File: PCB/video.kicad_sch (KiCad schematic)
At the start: 2 parts, among them U14 KM416x254, U15 KM416x254

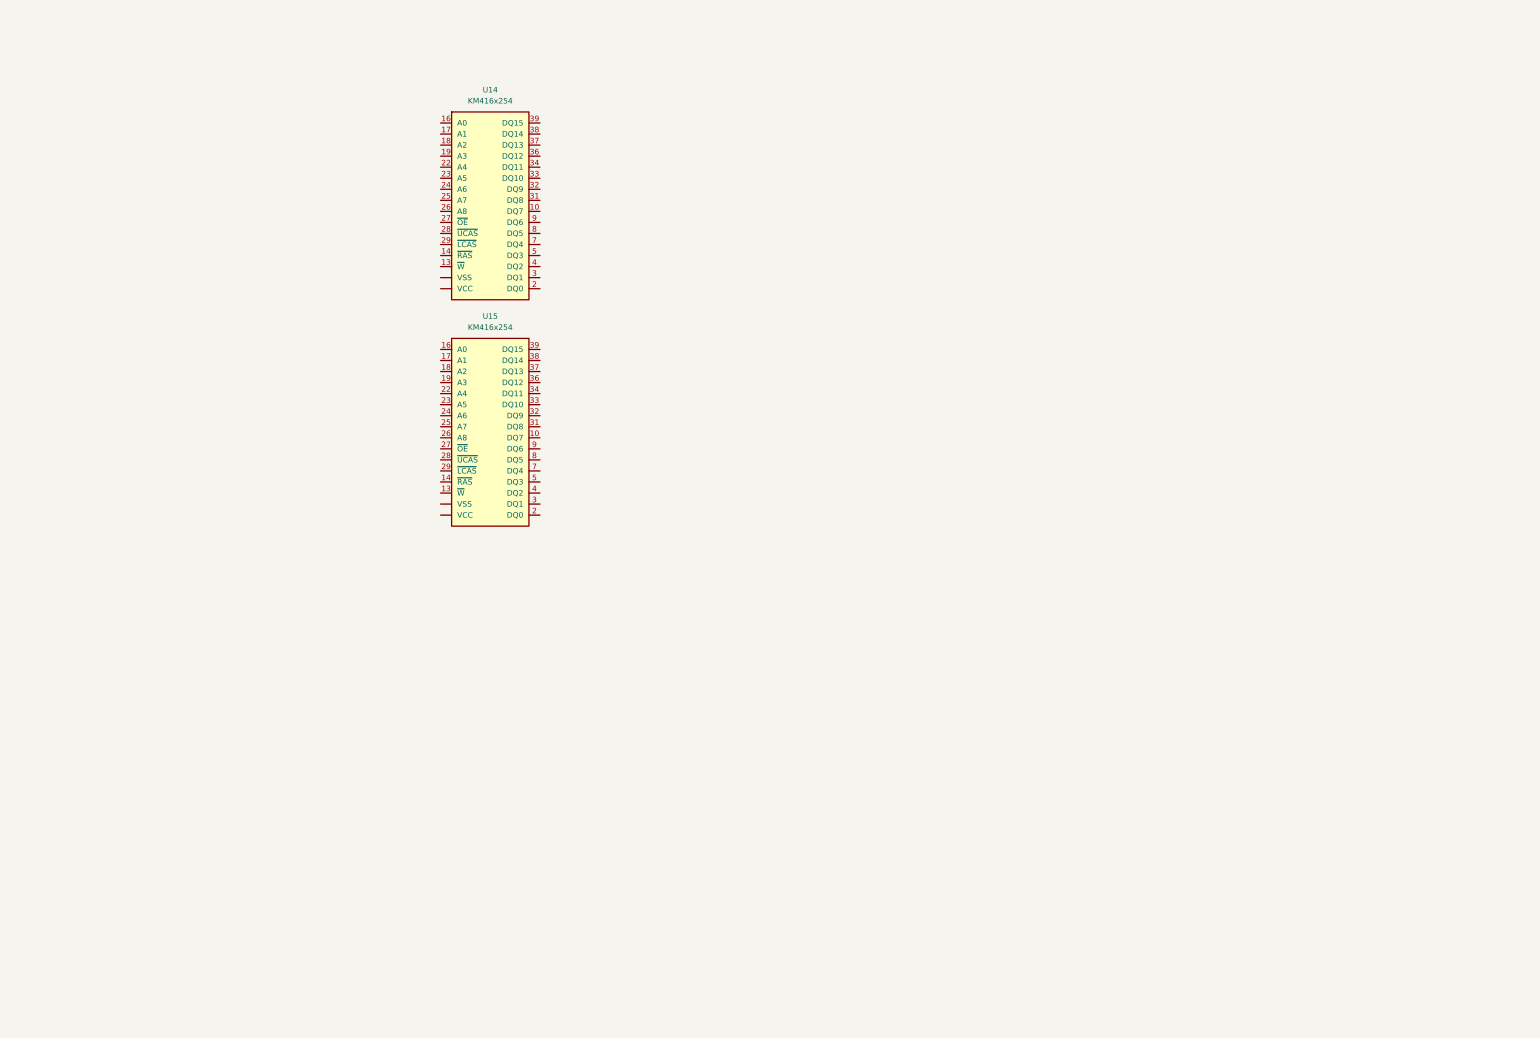
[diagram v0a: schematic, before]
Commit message: adding video chip and support bits
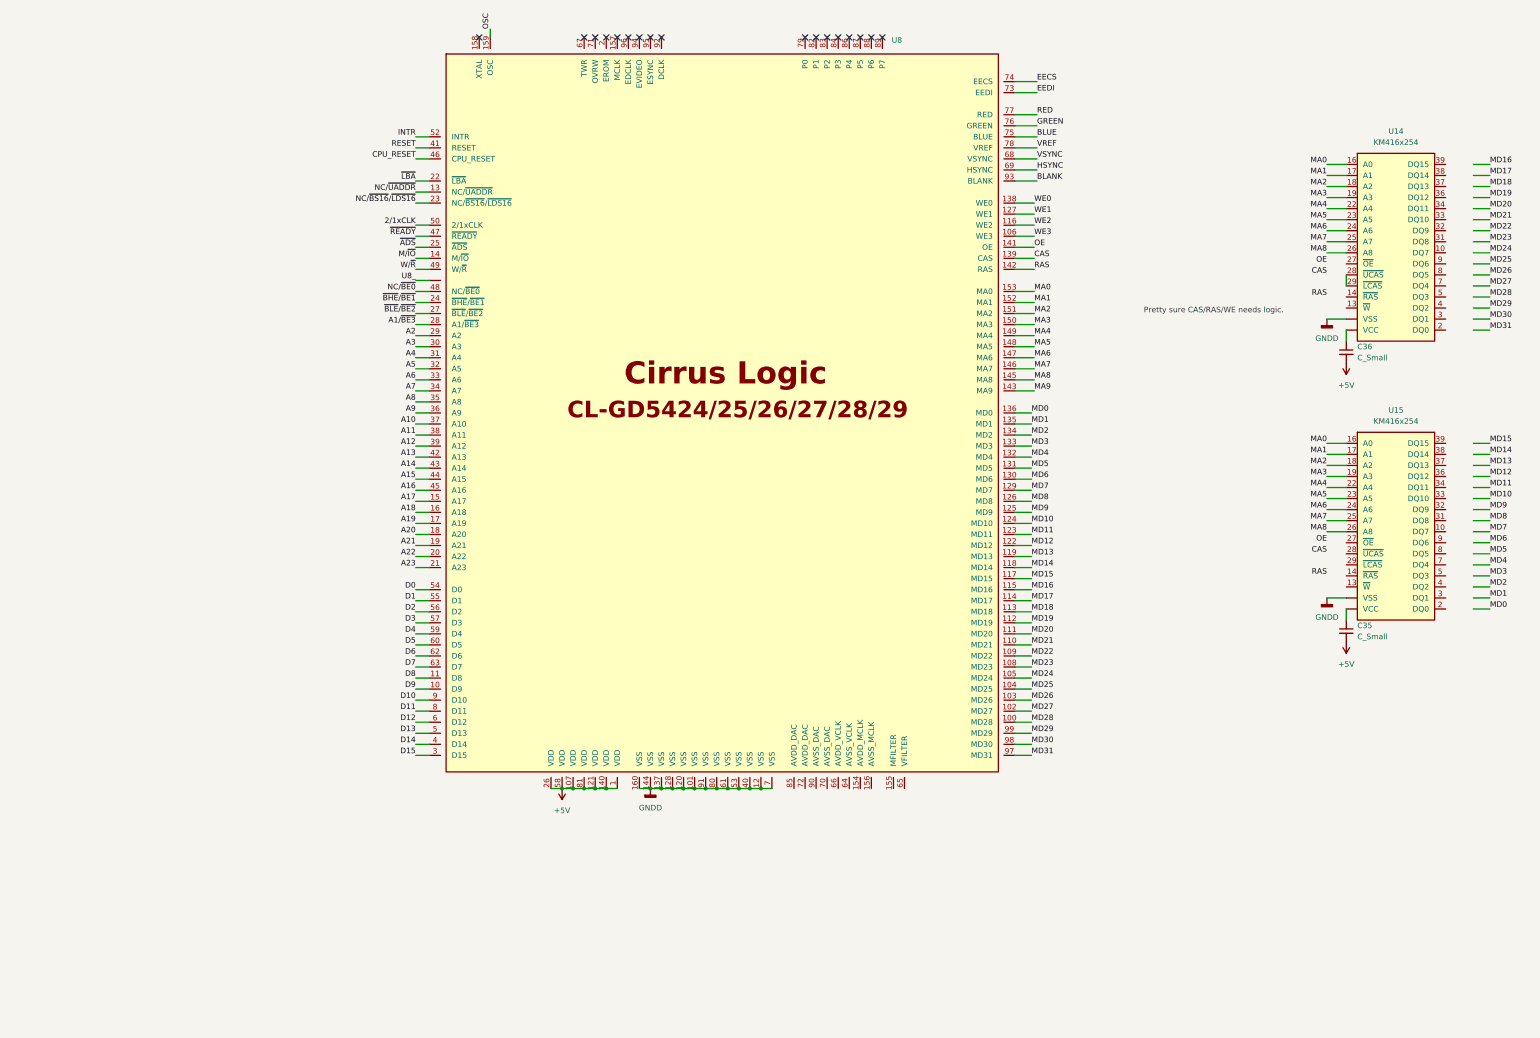
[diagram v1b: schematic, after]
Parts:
- added C35, C36: C_Small, symbol Device:C_Small
- added U8: CL-GD5428-LOCALBUS, Package_QFP:PQFP-160_28x28mm_P0.65mm, symbol CL-GD54xx:CL-GD542x
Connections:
- net at U15.1,6,20 (VCC): now also C35.1
- net MA0: now reaches U15.16 (A0)
- net MA0: now also U14.16 (A0), U8.153 (MA0)
- net MA1: now reaches U15.17 (A1)
- net MA1: now also U14.17 (A1), U8.152 (MA1)
- net MA2: now reaches U15.18 (A2)
- net MA2: now also U14.18 (A2), U8.151 (MA2)
- net MA3: now reaches U15.19 (A3)
- net MA3: now also U14.19 (A3), U8.150 (MA3)
- net GNDD: now reaches U15.21,35,40 (VSS)
- net GNDD: now also U14.21,35,40 (VSS), U8.101 (VSS), U8.12 (VSS), U8.120 (VSS), U8.128 (VSS), U8.137 (VSS), U8.144 (VSS), U8.160 (VSS), U8.40 (VSS), U8.53 (VSS), U8.61 (VSS), U8.7 (VSS), U8.80 (VSS), U8.91 (VSS)
- net MA4: now reaches U15.22 (A4)
- net MA4: now also U14.22 (A4), U8.149 (MA4)
- net MA5: now reaches U15.23 (A5)
- net MA5: now also U14.23 (A5), U8.148 (MA5)
- net MA6: now reaches U15.24 (A6)
- net MA6: now also U14.24 (A6), U8.147 (MA6)
- net MA7: now reaches U15.25 (A7)
- net MA7: now also U14.25 (A7), U8.146 (MA7)
- net MA8: now reaches U15.26 (A8)
- net MA8: now also U14.26 (A8), U8.145 (MA8)
- net at U14.1,6,20 (VCC): now also C36.1
- net at U14.28 (~{UCAS}): now also U14.29 (~{LCAS})
- new net +5V: C35.2, C36.2, U8.1 (VDD), U8.107 (VDD), U8.121 (VDD), U8.140 (VDD), U8.26 (VDD), U8.58 (VDD), U8.81 (VDD)
- new net 2/1xCLK: U8.50 (2/1xCLK)
- new net A1/~{BE3}: U8.28 (A1/~{BE3})
- new net A10: U8.37 (A10)
- new net A11: U8.38 (A11)
- new net A12: U8.39 (A12)
- new net A13: U8.42 (A13)
- new net A14: U8.43 (A14)
- new net A15: U8.44 (A15)
- new net A16: U8.45 (A16)
- new net A17: U8.15 (A17)
- new net A18: U8.16 (A18)
- new net A19: U8.17 (A19)
- new net A2: U8.29 (A2)
- new net A20: U8.18 (A20)
- new net A21: U8.19 (A21)
- new net A22: U8.20 (A22)
- new net A23: U8.21 (A23)
- new net A3: U8.30 (A3)
- new net A4: U8.31 (A4)
- new net A5: U8.32 (A5)
- new net A6: U8.33 (A6)
- new net A7: U8.34 (A7)
- new net A8: U8.35 (A8)
- new net A9: U8.36 (A9)
- new net BLANK: U8.93 (BLANK)
- new net BLUE: U8.75 (BLUE)
- new net CAS: U8.139 (CAS)
- new net CPU_RESET: U8.46 (CPU_RESET)
- new net D0: U8.54 (D0)
- new net D1: U8.55 (D1)
- new net D10: U8.9 (D10)
- new net D11: U8.8 (D11)
- new net D12: U8.6 (D12)
- new net D13: U8.5 (D13)
- new net D14: U8.4 (D14)
- new net D15: U8.3 (D15)
- new net D2: U8.56 (D2)
- new net D3: U8.57 (D3)
- new net D4: U8.59 (D4)
- new net D5: U8.60 (D5)
- new net D6: U8.62 (D6)
- new net D7: U8.63 (D7)
- new net D8: U8.11 (D8)
- new net D9: U8.10 (D9)
- new net EECS: U8.74 (EECS)
- new net EEDI: U8.73 (EEDI)
- new net GREEN: U8.76 (GREEN)
- new net HSYNC: U8.69 (HSYNC)
- new net INTR: U8.52 (INTR)
- new net M/~{IO}: U8.14 (M/~{IO})
- new net MA9: U8.143 (MA9)
- new net MD0: U8.136 (MD0)
- new net MD1: U8.135 (MD1)
- new net MD10: U8.124 (MD10)
- new net MD11: U8.123 (MD11)
- new net MD12: U8.122 (MD12)
- new net MD13: U8.119 (MD13)
- new net MD14: U8.118 (MD14)
- new net MD15: U8.117 (MD15)
- new net MD16: U8.115 (MD16)
- new net MD17: U8.114 (MD17)
- new net MD18: U8.113 (MD18)
- new net MD19: U8.112 (MD19)
- new net MD2: U8.134 (MD2)
- new net MD20: U8.111 (MD20)
- new net MD21: U8.110 (MD21)
- new net MD22: U8.109 (MD22)
- new net MD23: U8.108 (MD23)
- new net MD24: U8.105 (MD24)
- new net MD25: U8.104 (MD25)
- new net MD26: U8.103 (MD26)
- new net MD27: U8.102 (MD27)
- new net MD28: U8.100 (MD28)
- new net MD29: U8.99 (MD29)
- new net MD3: U8.133 (MD3)
- new net MD30: U8.98 (MD30)
- new net MD31: U8.97 (MD31)
- new net MD4: U8.132 (MD4)
- new net MD5: U8.131 (MD5)
- new net MD6: U8.130 (MD6)
- new net MD7: U8.129 (MD7)
- new net MD8: U8.126 (MD8)
- new net MD9: U8.125 (MD9)
- new net NC/~{BE0}: U8.48 (NC/~{BE0})
- new net NC/~{BS16}/~{LDS16}: U8.23 (NC/~{BS16}/~{LDS16})
- new net NC/~{UADDR}: U8.13 (NC/~{UADDR})
- new net OE: U8.141 (OE)
- new net OSC: U8.159 (OSC)
- new net RAS: U8.142 (RAS)
- new net RED: U8.77 (RED)
- new net RESET: U8.41 (RESET)
- new net U8_: U8.
- new net VREF: U8.78 (VREF)
- new net VSYNC: U8.68 (VSYNC)
- new net W/~{R}: U8.49 (W/~{R})
- new net WE0: U8.138 (WE0)
- new net WE1: U8.127 (WE1)
- new net WE2: U8.116 (WE2)
- new net WE3: U8.106 (WE3)
- new net ~{ADS}: U8.25 (~{ADS})
- new net ~{BHE}/~{BE1}: U8.24 (~{BHE}/~{BE1})
- new net ~{BLE}/~{BE2}: U8.27 (~{BLE}/~{BE2})
- new net ~{LBA}: U8.22 (~{LBA})
- new net ~{READY}: U8.47 (~{READY})
- no-connect marks 0 -> 17
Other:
- note added: "Pretty sure CAS/RAS/WE needs logic."
- moved on the sheet: U14, U15

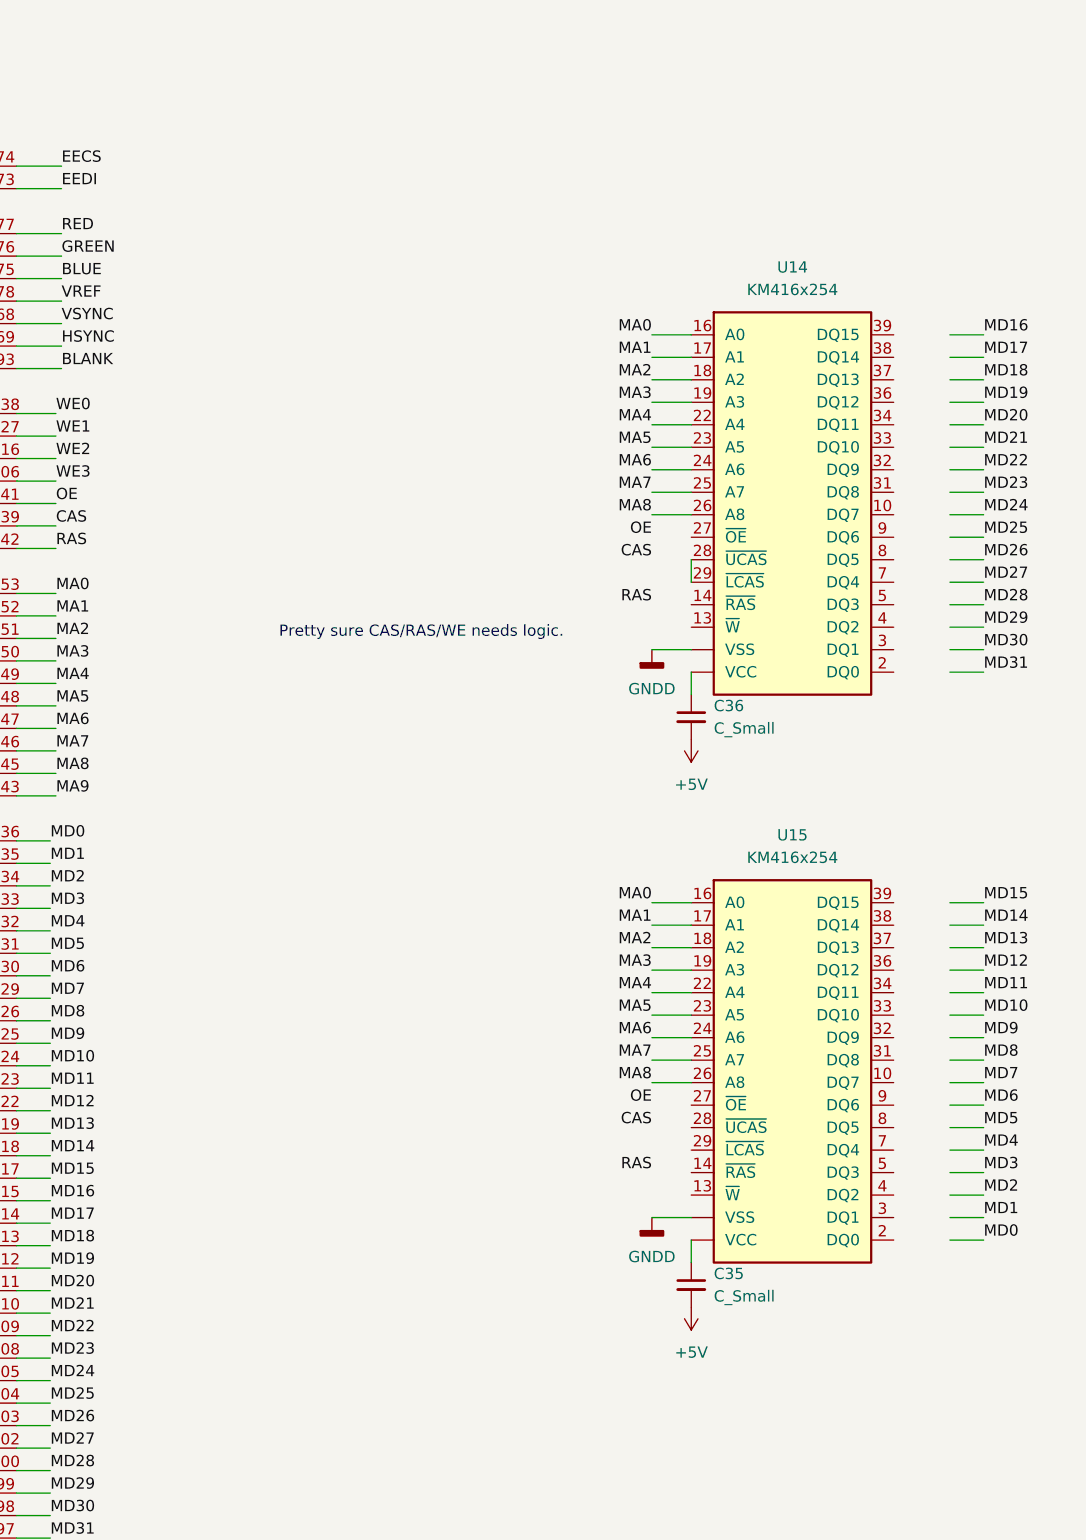
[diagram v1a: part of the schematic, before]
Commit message: dove into CAS/RAS/OE/WE muxing for Multi-cas 256x16 mem devices
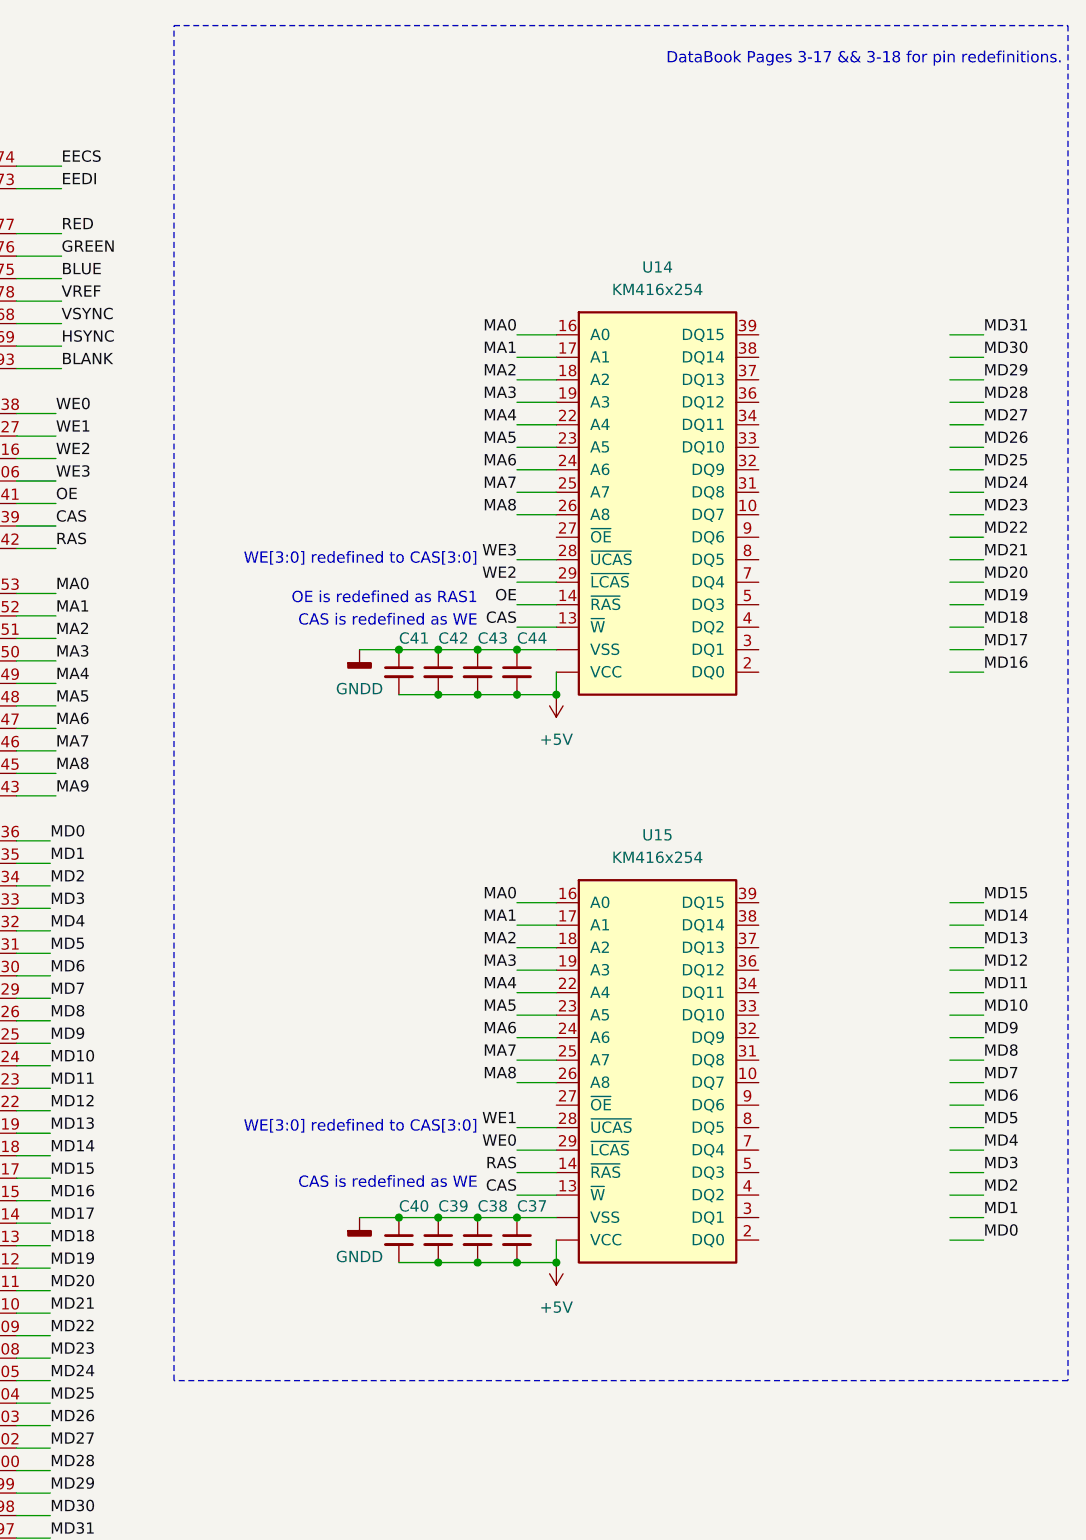
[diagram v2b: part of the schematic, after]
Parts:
- removed C35, C36: C_Small, symbol Device:C_Small
- added C37, C38, C39, C40, C41, C42, C43, C44: C_Small, symbol Device:C_Small
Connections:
- net +5V: now also U14.1,6,20 (VCC), U15.1,6,20 (VCC), C37.2, C38.2, C39.2, C40.2, C41.2, C42.2, C43.2, C44.2
- net CAS: now also U14.13 (~{W}), U15.13 (~{W})
- net GNDD: now also C37.1, C38.1, C39.1, C40.1, C41.1, C42.1, C43.1, C44.1
- net OE: now also U14.14 (~{RAS})
- net RAS: now also U15.14 (~{RAS})
- net WE0: now also U15.29 (~{LCAS})
- net WE1: now also U15.28 (~{UCAS})
- net WE2: now also U14.29 (~{LCAS})
- net WE3: now also U14.28 (~{UCAS})
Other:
- note added: "CAS is redefined as WE"
- note added: "DataBook Pages 3-17 && 3-18 for pin redefinitions."
- note added: "OE is redefined as RAS1"
- note added: "WE[3:0] redefined to CAS[3:0]"
- note removed: "Pretty sure CAS/RAS/WE needs logic."
- moved on the sheet: U14, U15

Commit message: started initial layout
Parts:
- added U16, U17: SN74ALVC164245DGG, Package_SO:TSSOP-48_6.1x12.5mm_P0.5mm, symbol 74xx:SN74ALVC164245DGG
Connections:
- net GNDD: now also U14.27 (~{OE}), U15.27 (~{OE}), U8.51 (ISA-0WS)
- net 2/1xCLK renamed CLK_CPU
- net A1/~{BE3} renamed ~{BE3}
- net CPU_RESET: no longer names the net of U8.46 (CPU_RESET)
- net EECS renamed ~{OE_L}
- net ~{OE_L}: now also U16.25 (2~{OE}), U16.48 (1~{OE})
- net EEDI renamed ~{OE_H}
- net ~{OE_H}: now also U17.25 (2~{OE}), U17.48 (1~{OE})
- net INTR: no longer names the net of U8.52 (INTR)
- net M/~{IO} renamed M~{IO}
- net NC/~{BE0} renamed ~{BE0}
- net NC/~{BS16}/~{LDS16} renamed ~{BS16}
- net NC/~{UADDR} renamed ~{UADDR_VGA}
- net RESET: no longer names the net of U8.41 (RESET)
- removed net U8_: U8.
- net W/~{R} renamed W~{R}
- net ~{ADS} renamed ~{RDY_CPU}
- net ~{BHE}/~{BE1} renamed ~{BE1}
- net ~{BLE}/~{BE2} renamed ~{BE2}
- net ~{LBA} renamed ~{LBA_VGA}
- net ~{READY} renamed ~{ADS_CPU}
- new net: U16.10 (GND), U16.15 (GND), U16.21 (GND), U16.28 (GND), U16.34 (GND), U16.39 (GND), U16.4 (GND), U16.45 (GND)
- new net: U16.18 (V_{CC(B)}), U16.7 (V_{CC(B)})
- new net: U16.31 (V_{CC(A)}), U16.42 (V_{CC(A)})
- new net: U17.10 (GND), U17.15 (GND), U17.21 (GND), U17.28 (GND), U17.34 (GND), U17.39 (GND), U17.4 (GND), U17.45 (GND)
- new net: U17.18 (V_{CC(B)}), U17.7 (V_{CC(B)})
- new net: U17.31 (V_{CC(A)}), U17.42 (V_{CC(A)})
- new net 1A0: U16.47 (1A0), U17.47 (1A0)
- new net 1A1: U16.46 (1A1), U17.46 (1A1)
- new net 1A2: U16.44 (1A2), U17.44 (1A2)
- new net 1A3: U16.43 (1A3), U17.43 (1A3)
- new net 1A4: U16.41 (1A4), U17.41 (1A4)
- new net 1A5: U16.40 (1A5), U17.40 (1A5)
- new net 1A6: U16.38 (1A6), U17.38 (1A6)
- new net 1A7: U16.37 (1A7), U17.37 (1A7)
- new net 2A0: U16.36 (2A0), U17.36 (2A0)
- new net 2A1: U16.35 (2A1), U17.35 (2A1)
- new net 2A2: U16.33 (2A2), U17.33 (2A2)
- new net 2A3: U16.32 (2A3), U17.32 (2A3)
- new net 2A4: U16.30 (2A4), U17.30 (2A4)
- new net 2A5: U16.29 (2A5), U17.29 (2A5)
- new net 2A6: U16.27 (2A6), U17.27 (2A6)
- new net 2A7: U16.26 (2A7), U17.26 (2A7)
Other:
- moved on the sheet: C37, C38, C39, C40, C41, C42, C43, C44, U14, U15
